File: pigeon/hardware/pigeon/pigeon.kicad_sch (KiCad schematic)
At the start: 17 parts, among them J1 Battery, SW1 Power Switch, SW2 Mode Switch, U1 ESP32-S3-Zero, U2 Adafruit_Ultimate_GPS, U3 Adafruit_RFM95W

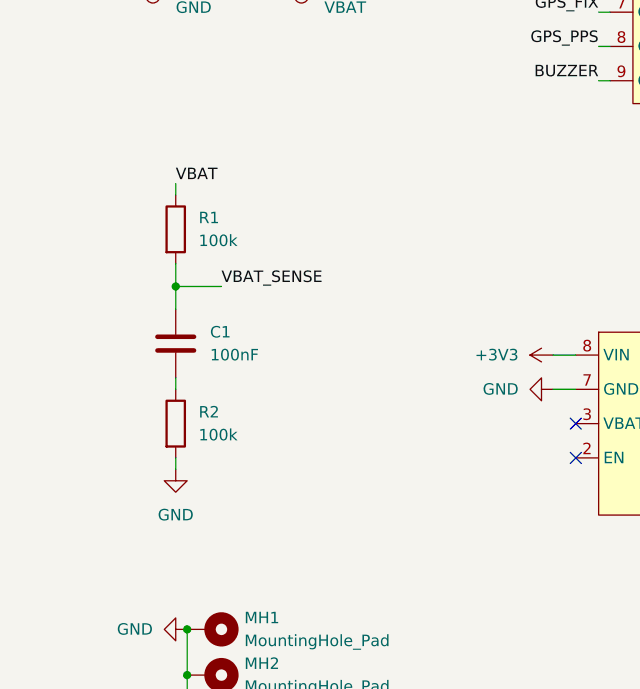
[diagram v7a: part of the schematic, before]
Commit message: pigeon: fixed voltage divider by putting C1 parralel with R2
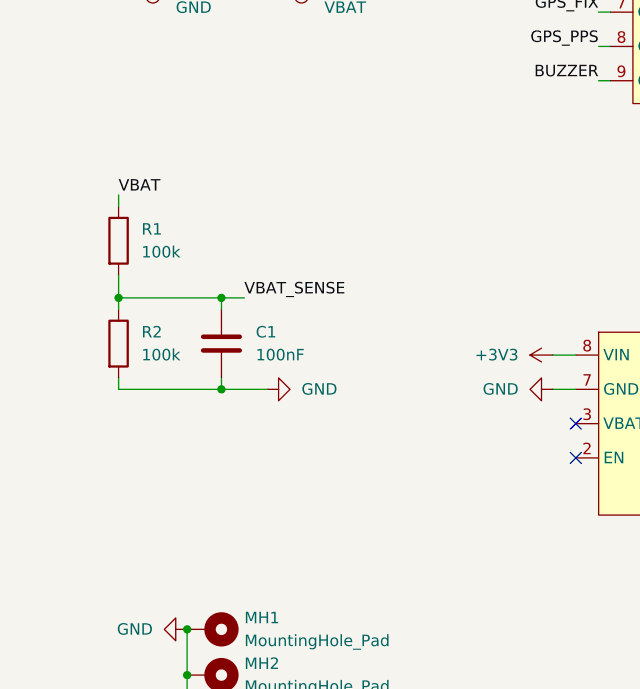
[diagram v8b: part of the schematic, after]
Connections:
- net GND: now also C1.2
- net VBAT_SENSE: now also R2.1
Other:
- moved on the sheet: C1, R1, R2
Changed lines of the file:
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@@
 	(paper "A4")
 	(junction
-		(at 48.26 40.64)
+		(at 27.94 90.17)
 		(diameter 0)
 		(color 0 0 0 0)
 	)
 	(junction
-		(at 31.75 40.64)
+		(at 48.26 40.64)
 		(diameter 0)
 		(color 0 0 0 0)
 	)
 	(junction
-		(at 34.29 88.9)
+		(at 31.75 40.64)
 		(diameter 0)
 		(color 0 0 0 0)
@@
 	)
 	(junction
+		(at 39.37 100.33)
+		(diameter 0)
+		(color 0 0 0 0)
+	)
+	(junction
 		(at 31.75 49.53)
 		(diameter 0)
 		(color 0 0 0 0)
 	)
+	(junction
+		(at 39.37 90.17)
+		(diameter 0)
+		(color 0 0 0 0)
+	)
 	(no_connect
 		(at 78.74 104.14)
@@
 	(wire
 		(pts
-			(xy 34.29 88.9) (xy 39.37 88.9)
+			(xy 27.94 90.17) (xy 39.37 90.17)
 		)
 		(stroke
@@
 	(wire
 		(pts
+			(xy 27.94 99.06) (xy 27.94 100.33)
+		)
+		(stroke
+			(width 0)
+			(type default)
+		)
+	)
+	(wire
+		(pts
 			(xy 181.61 36.83) (xy 180.34 36.83)
 		)
@@
 	(wire
 		(pts
+			(xy 39.37 100.33) (xy 27.94 100.33)
+		)
+		(stroke
+			(width 0)
+			(type default)
+		)
+	)
+	(wire
+		(pts
 			(xy 113.03 50.8) (xy 111.76 50.8)
 		)
@@
 	(wire
 		(pts
+			(xy 44.45 100.33) (xy 39.37 100.33)
+		)
+		(stroke
+			(width 0)
+			(type default)
+		)
+	)
+	(wire
+		(pts
 			(xy 57.15 40.64) (xy 62.23 40.64)
 		)
@@
 	(wire
 		(pts
-			(xy 34.29 86.36) (xy 34.29 88.9)
+			(xy 27.94 87.63) (xy 27.94 90.17)
 		)
 		(stroke
@@
 	(wire
 		(pts
-			(xy 48.26 53.34) (xy 48.26 40.64)
+			(xy 39.37 90.17) (xy 39.37 91.44)
 		)
 		(stroke
@@
 	(wire
 		(pts
-			(xy 31.75 49.53) (xy 31.75 40.64)
+			(xy 48.26 53.34) (xy 48.26 40.64)
 		)
 		(stroke
@@
 	(wire
 		(pts
-			(xy 35.56 127) (xy 35.56 132.08)
+			(xy 31.75 49.53) (xy 31.75 40.64)
 		)
 		(stroke
@@
 	(wire
 		(pts
-			(xy 181.61 40.64) (xy 180.34 40.64)
+			(xy 35.56 127) (xy 35.56 132.08)
 		)
 		(stroke
@@
 	(wire
 		(pts
-			(xy 34.29 77.47) (xy 34.29 78.74)
+			(xy 181.61 40.64) (xy 180.34 40.64)
 		)
 		(stroke
@@
 	(wire
 		(pts
-			(xy 34.29 88.9) (xy 34.29 91.44)
+			(xy 27.94 78.74) (xy 27.94 80.01)
 		)
 		(stroke
@@
 	(wire
 		(pts
-			(xy 143.51 40.64) (xy 144.78 40.64)
+			(xy 41.91 90.17) (xy 39.37 90.17)
 		)
 		(stroke
@@
 	(wire
 		(pts
-			(xy 29.21 40.64) (xy 31.75 40.64)
+			(xy 27.94 90.17) (xy 27.94 91.44)
 		)
 		(stroke
@@
 	(wire
 		(pts
-			(xy 81.28 50.8) (xy 82.55 50.8)
+			(xy 143.51 40.64) (xy 144.78 40.64)
 		)
 		(stroke
@@
 	(wire
 		(pts
-			(xy 81.28 58.42) (xy 82.55 58.42)
+			(xy 29.21 40.64) (xy 31.75 40.64)
 		)
 		(stroke
@@
 	(wire
 		(pts
-			(xy 35.56 132.08) (xy 35.56 137.16)
+			(xy 81.28 50.8) (xy 82.55 50.8)
 		)
 		(stroke
@@
 	(wire
 		(pts
-			(xy 143.51 55.88) (xy 144.78 55.88)
+			(xy 81.28 58.42) (xy 82.55 58.42)
 		)
 		(stroke
@@
 	(wire
 		(pts
-			(xy 100.33 27.94) (xy 100.33 30.48)
+			(xy 35.56 132.08) (xy 35.56 137.16)
 		)
 		(stroke
@@
 	(wire
 		(pts
-			(xy 34.29 109.22) (xy 34.29 107.95)
+			(xy 143.51 55.88) (xy 144.78 55.88)
 		)
 		(stroke
@@
 	(wire
 		(pts
-			(xy 34.29 100.33) (xy 34.29 99.06)
+			(xy 100.33 27.94) (xy 100.33 30.48)
 		)
 		(stroke
@@
 	(wire
 		(pts
+			(xy 39.37 100.33) (xy 39.37 99.06)
+		)
+		(stroke
+			(width 0)
+			(type default)
+		)
+	)
+	(wire
+		(pts
 			(xy 143.51 48.26) (xy 144.78 48.26)
 		)
@@
 	)
 	(label "VBAT_SENSE"
-		(at 39.37 88.9 0)
+		(at 41.91 90.17 0)
 		(effects
 			(font
@@
 	)
 	(label "VBAT"
-		(at 34.29 77.47 0)
+		(at 27.94 78.74 0)
 		(effects
 			(font
@@
 	(symbol
 		(lib_id "power:GND")
-		(at 34.29 109.22 0)
+		(at 44.45 100.33 90)
 		(unit 1)
 		(body_style 1)
@@
 		(fields_autoplaced yes)
 		(property "Reference" "#PWR04"
-			(at 34.29 115.57 0)
+			(at 50.8 100.33 0)
 			(hide yes)
 			(show_name no)
@@
 		)
 		(property "Value" "GND"
-			(at 34.29 114.3 0)
+			(at 48.26 100.3299 90)
 			(show_name no)
 			(do_not_autoplace no)
@@
 					(size 1.27 1.27)
 				)
+				(justify right)
 			)
 		)
 		(property "Footprint" ""
-			(at 34.29 109.22 0)
+			(at 44.45 100.33 0)
 			(hide yes)
 			(show_name no)
@@
 		)
 		(property "Datasheet" ""
-			(at 34.29 109.22 0)
+			(at 44.45 100.33 0)
 			(hide yes)
 			(show_name no)
@@
 		)
 		(property "Description" "Power symbol creates a global label with name \"GND\" , ground"
-			(at 34.29 109.22 0)
+			(at 44.45 100.33 0)
 			(hide yes)
 			(show_name no)
@@
 	(symbol
 		(lib_id "Device:R")
-		(at 34.29 82.55 0)
+		(at 27.94 83.82 0)
 		(unit 1)
 		(body_style 1)
@@
 		(fields_autoplaced yes)
 		(property "Reference" "R1"
-			(at 36.83 81.2799 0)
+			(at 30.48 82.5499 0)
 			(show_name no)
 			(do_not_autoplace no)
@@
 		)
 		(property "Value" "100k"
-			(at 36.83 83.8199 0)
+			(at 30.48 85.0899 0)
 			(show_name no)
 			(do_not_autoplace no)
@@
 		)
 		(property "Footprint" "Resistor_SMD:R_0805_2012Metric_Pad1.20x1.40mm_HandSolder"
-			(at 32.512 82.55 90)
+			(at 26.162 83.82 90)
 			(hide yes)
 			(show_name no)
@@
 		)
 		(property "Datasheet" ""
-			(at 34.29 82.55 0)
+			(at 27.94 83.82 0)
 			(hide yes)
 			(show_name no)
@@
 		)
 		(property "Description" "Resistor"
-			(at 34.29 82.55 0)
+			(at 27.94 83.82 0)
 			(hide yes)
 			(show_name no)
@@
 	(symbol
 		(lib_id "Device:C")
-		(at 34.29 95.25 0)
+		(at 39.37 95.25 0)
 		(unit 1)
 		(body_style 1)
@@
 		(fields_autoplaced yes)
 		(property "Reference" "C1"
-			(at 38.1 93.9799 0)
+			(at 43.18 93.9799 0)
 			(show_name no)
 			(do_not_autoplace no)
@@
 		)
 		(property "Value" "100nF"
-			(at 38.1 96.5199 0)
+			(at 43.18 96.5199 0)
 			(show_name no)
 			(do_not_autoplace no)
@@
 		)
 		(property "Footprint" "Capacitor_SMD:C_0805_2012Metric_Pad1.18x1.45mm_HandSolder"
-			(at 35.2552 99.06 0)
+			(at 40.3352 99.06 0)
 			(hide yes)
 			(show_name no)
@@
 		)
 		(property "Datasheet" ""
-			(at 34.29 95.25 0)
+			(at 39.37 95.25 0)
 			(hide yes)
 			(show_name no)
@@
 		)
 		(property "Description" "Unpolarized capacitor"
-			(at 34.29 95.25 0)
+			(at 39.37 95.25 0)
 			(hide yes)
 			(show_name no)
@@
 	(symbol
 		(lib_id "Device:R")
-		(at 34.29 104.14 0)
+		(at 27.94 95.25 0)
 		(unit 1)
 		(body_style 1)
@@
 		(dnp no)
 		(property "Reference" "R2"
-			(at 36.83 102.8699 0)
+			(at 30.48 93.9799 0)
 			(show_name no)
 			(do_not_autoplace no)
@@
 		)
 		(property "Value" "100k"
-			(at 36.83 105.4099 0)
+			(at 30.48 96.5199 0)
 			(show_name no)
 			(do_not_autoplace no)
@@
 		)
 		(property "Footprint" "Resistor_SMD:R_0805_2012Metric_Pad1.20x1.40mm_HandSolder"
-			(at 32.512 104.14 90)
+			(at 26.162 95.25 90)
 			(hide yes)
 			(show_name no)
@@
 		)
 		(property "Datasheet" ""
-			(at 34.29 104.14 0)
+			(at 27.94 95.25 0)
 			(hide yes)
 			(show_name no)
@@
 		)
 		(property "Description" "Resistor"
-			(at 34.29 104.14 0)
+			(at 27.94 95.25 0)
 			(hide yes)
 			(show_name no)
